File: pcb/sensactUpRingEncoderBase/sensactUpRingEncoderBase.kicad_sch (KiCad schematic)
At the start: 59 parts, among them J3 BaseConnector, J5 ToBase, SW1 SW_Push, SW2 TERM ON OFF, SW3 RotaryEncoder, U27 TPS54202DDC, U4 AMS1117-3.3, U5 74AHCT1G125

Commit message: Layout Improvements, added VCML4040
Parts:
- SW1: footprint Button_Switch_THT:SW_PUSH_6mm_H4.3mm -> liebler_MECH:Button_12mm_ANCHOR_CENTER
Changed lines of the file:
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@@
 			)
 		)
-		(property "Footprint" "Button_Switch_THT:SW_PUSH_6mm_H4.3mm"
+		(property "Footprint" "liebler_MECH:Button_12mm_ANCHOR_CENTER"
 			(at 132.08 72.39 0)
 			(effects

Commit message: Various updates in sensactRingEncoder
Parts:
- added H3, H4, H5: MountingHole, MountingHole:MountingHole_2.2mm_M2, symbol Mechanical:MountingHole
- added J1: ROT_EXT, Connector_PinHeader_2.54mm:PinHeader_1x03_P2.54mm_Vertical, symbol Connector_Generic:Conn_01x03
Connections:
- net A: now also J1.3 (Pin_3)
- net B: now also J1.1 (Pin_1)
- net GND: now also J1.2 (Pin_2)
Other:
- moved on the sheet: SW3

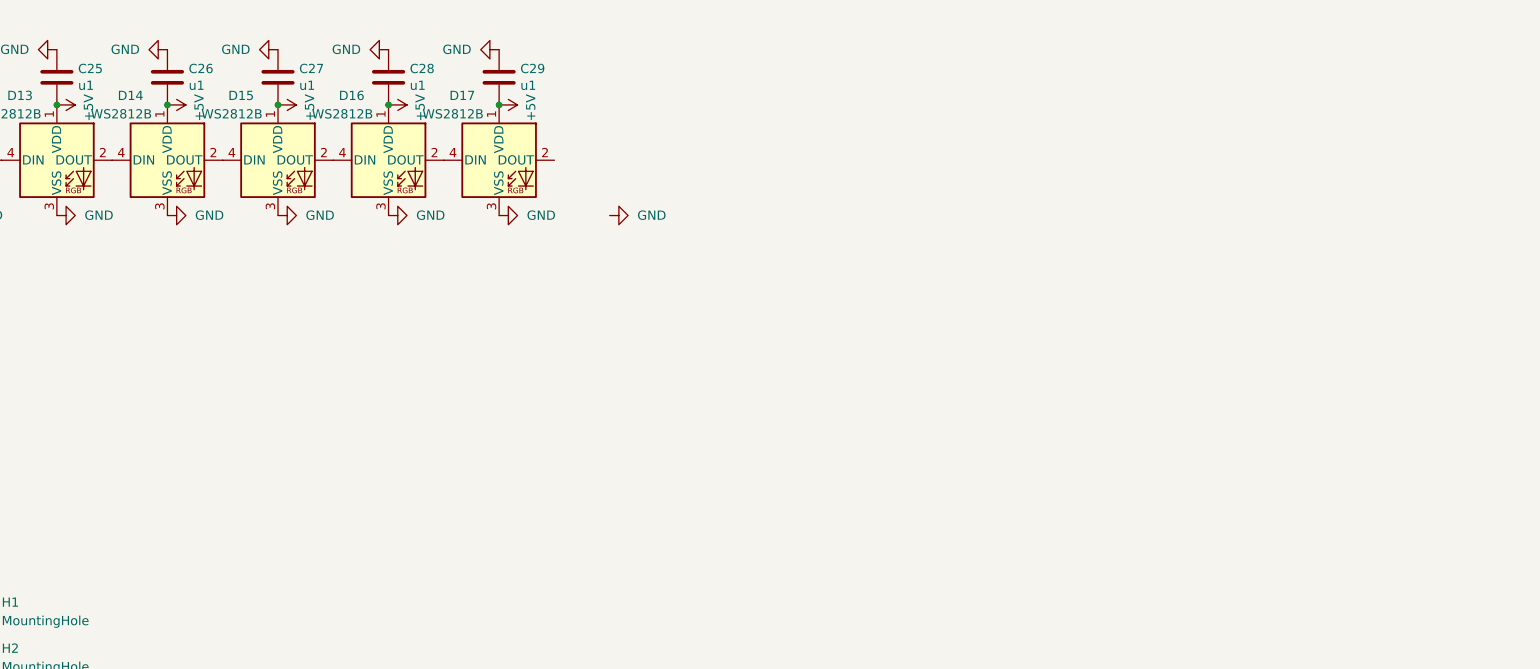
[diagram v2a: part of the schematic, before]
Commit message: sensactRingEncoder as ordered @ JLCPCB
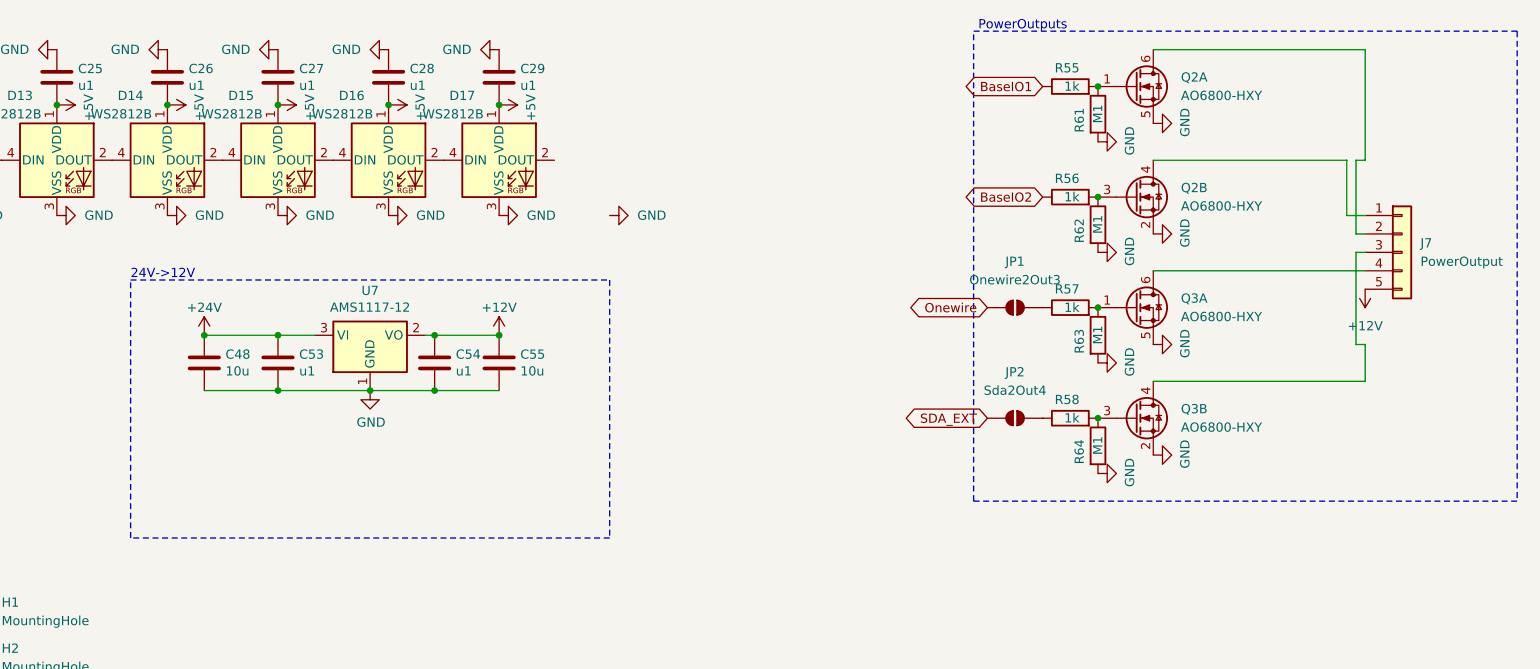
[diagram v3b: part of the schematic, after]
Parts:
- added C48, C55: 10u, Capacitor_SMD:C_0805_2012Metric_Pad1.18x1.45mm_HandSolder, symbol Device:C
- added C53, C54: u1, Capacitor_SMD:C_0805_2012Metric_Pad1.18x1.45mm_HandSolder, symbol Device:C
- added J7: PowerOutput, Connector_PinHeader_2.54mm:PinHeader_1x05_P2.54mm_Vertical, symbol Connector_Generic:Conn_01x05
- added JP1: Onewire2Out3, Jumper:SolderJumper-2_P1.3mm_Open_RoundedPad1.0x1.5mm, symbol Jumper:SolderJumper_2_Open
- added JP2: Sda2Out4, Jumper:SolderJumper-2_P1.3mm_Open_RoundedPad1.0x1.5mm, symbol Jumper:SolderJumper_2_Open
- added Q2, Q3: AO6800-HXY, Package_TO_SOT_SMD:SOT-23-6_Handsoldering, symbol Transistor_FET:Q_Dual_NMOS_G1S2G2D2S1D1
- added R55, R56, R57, R58: 1k, Resistor_SMD:R_0805_2012Metric_Pad1.20x1.40mm_HandSolder, symbol Device:R
- added R61, R62, R63, R64: M1, Resistor_SMD:R_0805_2012Metric_Pad1.20x1.40mm_HandSolder, symbol Device:R
- added U7: AMS1117-12, liebler_SEMICONDUCTORS:SOT-223-3_TabPin2_HANDSOLDER, symbol Regulator_Linear:AMS1117-3.3
- J1: footprint Connector_PinHeader_2.54mm:PinHeader_1x03_P2.54mm_Vertical -> liebler_CONN:PhoenixContact_MCV_1,5_3-G-3.5_1x03_P3.50mm_Vertical_smallerCourtyard
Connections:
- net +24V: now also C48.1, C53.1, U7.3 (VI)
- net BaseIO1: now also R55.1
- net BaseIO2: now also R56.1
- net GND: now also C48.2, C53.2, C54.2, C55.2, Q2.2 (S), Q2.5 (S), Q3.2 (S), Q3.5 (S), R61.2, R62.2, R63.2, R64.2, U7.1 (GND)
- net Onewire: now also JP1.1 (A)
- net SDA_EXT: now also JP2.1 (A)
- new net: Q2.3 (G), R56.2, R62.1
- new net: Q3.3 (G), R58.2, R64.1
- new net: J7.3 (Pin_3), Q3.4 (D)
- new net: JP1.2 (B), R57.1
- new net: Q3.1 (G), R57.2, R63.1
- new net: J7.1 (Pin_1), Q2.4 (D)
- new net: Q2.1 (G), R55.2, R61.1
- new net: J7.2 (Pin_2), Q2.6 (D)
- new net: JP2.2 (B), R58.1
- new net: J7.4 (Pin_4), Q3.6 (D)
- new net +12V: C54.1, C55.1, J7.5 (Pin_5), U7.2 (VO)
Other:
- note added: "24V->12V"
- note added: "PowerOutputs"
